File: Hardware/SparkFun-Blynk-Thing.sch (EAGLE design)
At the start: 103 parts, among them IC1 LMV358, Q1 2.5A/30V, Q2 MMBT2222A, Q3 MMBT2222A, U1 MCP73831, U2 ESP8266, U3 AP2112K-3.3V, U4 FT231XS-U, U5 W25Q32FVSS, U6 SI7021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

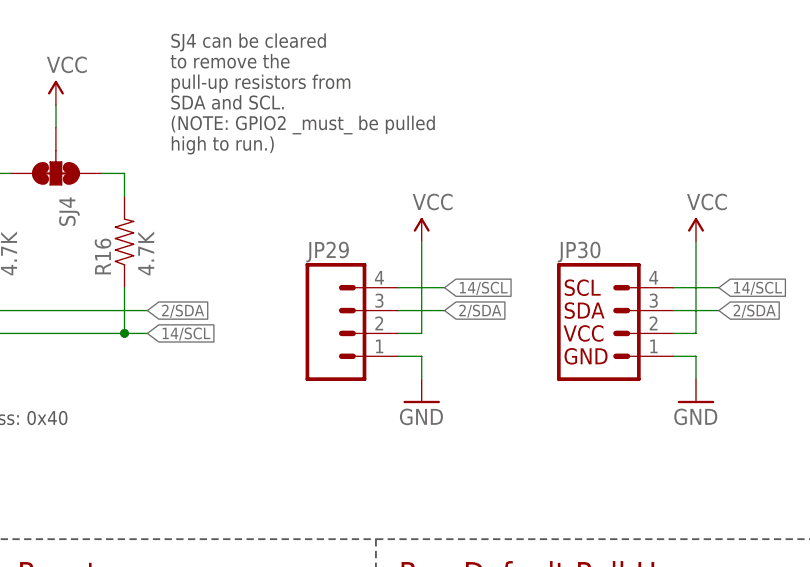
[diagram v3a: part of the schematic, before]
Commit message: Swapping JST connectors on I2C footprint.
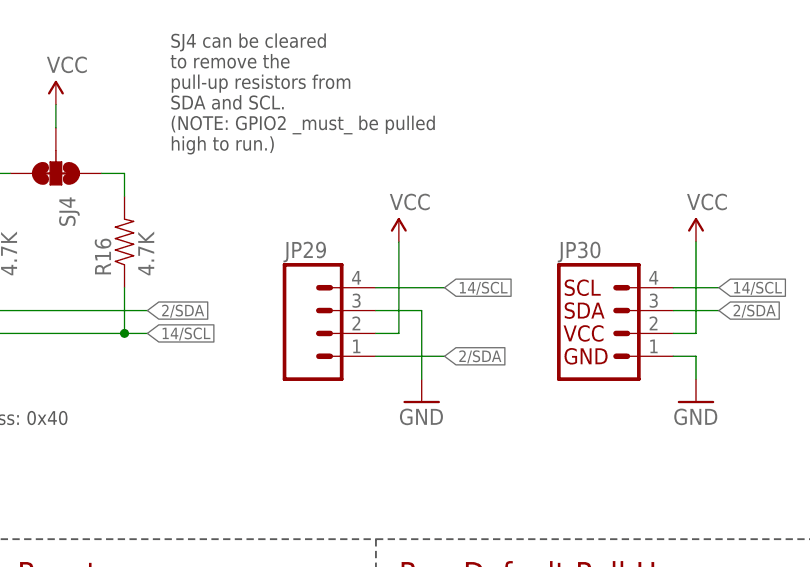
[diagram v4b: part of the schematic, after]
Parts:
- JP29: device SparkFun-Connectors:M04JST -> SparkFun-Connectors:M04JST-PTH-VERT
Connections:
- net 2/SDA: now also JP29.1; no longer JP29.3
- net GND: now also JP29.3; no longer JP29.1
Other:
- moved on the sheet: JP29
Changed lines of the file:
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@@
 <part name="JP4" library="blynk-thing-temp" deviceset="M01" device="ALLIGATOR_HALF" value=""/>
 <part name="JP6" library="blynk-thing-temp" deviceset="M01" device="ALLIGATOR_HALF" value=""/>
-<part name="JP29" library="SparkFun-Connectors" deviceset="M04" device="JST"/>
 <part name="D4" library="SparkFun-LED" deviceset="WS2812B" device="" value="WS2812"/>
 <part name="JP14" library="SparkFun-Connectors" deviceset="M03" device="JST-PTH-VERT">
@@
 <part name="S1" library="SparkFun-Electromechanical" deviceset="SWITCH-MOMENTARY-2" device="SMD-REDUNDANT" value=""/>
 <part name="GND34" library="SparkFun-Aesthetics" deviceset="GND" device=""/>
-<part name="GND38" library="SparkFun-Aesthetics" deviceset="GND" device=""/>
-<part name="SUPPLY19" library="SparkFun-Aesthetics" deviceset="VCC" device=""/>
 <part name="JP13" library="SparkFun-Connectors" deviceset="M01" device="PTH_NO_SILK_YES_STOP"/>
 <part name="JP21" library="SparkFun-Connectors" deviceset="M01" device="PTH_NO_SILK_YES_STOP"/>
@@
 <part name="SUPPLY1" library="SparkFun-Aesthetics" deviceset="VCC" device=""/>
 <part name="GND6" library="SparkFun-Aesthetics" deviceset="GND" device=""/>
+<part name="JP29" library="SparkFun-Connectors" deviceset="M04" device="JST-PTH-VERT"/>
+<part name="SUPPLY3" library="SparkFun-Aesthetics" deviceset="VCC" device=""/>
+<part name="GND42" library="SparkFun-Aesthetics" deviceset="GND" device=""/>
 </parts>
 <sheets>
@@
 <instance part="JP4" gate="G$1" x="165.1" y="101.6"/>
 <instance part="JP6" gate="G$1" x="165.1" y="81.28"/>
-<instance part="JP29" gate="G$1" x="378.46" y="160.02"/>
 <instance part="D4" gate="G$1" x="121.92" y="160.02" rot="MR0"/>
 <instance part="JP14" gate="G$1" x="149.86" y="160.02" smashed="yes" rot="R180">
@@
 <instance part="S1" gate="G$1" x="254" y="175.26"/>
 <instance part="GND34" gate="1" x="261.62" y="170.18"/>
-<instance part="GND38" gate="1" x="386.08" y="152.4"/>
-<instance part="SUPPLY19" gate="G$1" x="386.08" y="170.18"/>
 <instance part="JP13" gate="G$1" x="165.1" y="7.62"/>
 <instance part="JP21" gate="G$1" x="198.12" y="71.12"/>
@@
 <instance part="SUPPLY1" gate="G$1" x="17.78" y="185.42"/>
 <instance part="GND6" gate="1" x="17.78" y="162.56"/>
+<instance part="JP29" gate="G$1" x="375.92" y="160.02"/>
+<instance part="SUPPLY3" gate="G$1" x="383.54" y="170.18"/>
+<instance part="GND42" gate="1" x="386.08" y="152.4"/>
 </instances>
 <busses>
@@
 </segment>
 <segment>
-<pinref part="JP29" gate="G$1" pin="2"/>
-<wire x1="383.54" y1="160.02" x2="386.08" y2="160.02" width="0.1524" layer="91"/>
-<wire x1="386.08" y1="160.02" x2="386.08" y2="170.18" width="0.1524" layer="91"/>
-<pinref part="SUPPLY19" gate="G$1" pin="VCC"/>
-</segment>
-<segment>
 <pinref part="R12" gate="G$1" pin="1"/>
 <pinref part="SUPPLY24" gate="G$1" pin="VCC"/>
@@
 <pinref part="SUPPLY1" gate="G$1" pin="VCC"/>
 <wire x1="17.78" y1="185.42" x2="17.78" y2="182.88" width="0.1524" layer="91"/>
+</segment>
+<segment>
+<pinref part="JP29" gate="G$1" pin="2"/>
+<wire x1="381" y1="160.02" x2="383.54" y2="160.02" width="0.1524" layer="91"/>
+<wire x1="383.54" y1="160.02" x2="383.54" y2="170.18" width="0.1524" layer="91"/>
+<pinref part="SUPPLY3" gate="G$1" pin="VCC"/>
 </segment>
 </net>
@@
 </segment>
 <segment>
-<pinref part="JP29" gate="G$1" pin="1"/>
-<wire x1="383.54" y1="157.48" x2="386.08" y2="157.48" width="0.1524" layer="91"/>
-<wire x1="386.08" y1="157.48" x2="386.08" y2="154.94" width="0.1524" layer="91"/>
-<pinref part="GND38" gate="1" pin="GND"/>
-</segment>
-<segment>
 <pinref part="R11" gate="G$1" pin="2"/>
 <pinref part="GND18" gate="1" pin="GND"/>
@@
 <pinref part="GND6" gate="1" pin="GND"/>
 <wire x1="17.78" y1="165.1" x2="17.78" y2="167.64" width="0.1524" layer="91"/>
+</segment>
+<segment>
+<pinref part="JP29" gate="G$1" pin="3"/>
+<wire x1="381" y1="162.56" x2="386.08" y2="162.56" width="0.1524" layer="91"/>
+<wire x1="386.08" y1="162.56" x2="386.08" y2="154.94" width="0.1524" layer="91"/>
+<pinref part="GND42" gate="1" pin="GND"/>
 </segment>
 </net>
@@
 </segment>
 <segment>
-<pinref part="JP29" gate="G$1" pin="3"/>
-<wire x1="383.54" y1="162.56" x2="388.62" y2="162.56" width="0.1524" layer="91"/>
-<label x="388.62" y="162.56" size="1.27" layer="95" xref="yes"/>
-</segment>
-<segment>
 <pinref part="JP30" gate="G$1" pin="3"/>
 <wire x1="414.02" y1="162.56" x2="419.1" y2="162.56" width="0.1524" layer="91"/>
 <label x="419.1" y="162.56" size="1.27" layer="95" xref="yes"/>
+</segment>
+<segment>
+<pinref part="JP29" gate="G$1" pin="1"/>
+<wire x1="381" y1="157.48" x2="388.62" y2="157.48" width="0.1524" layer="91"/>
+<label x="388.62" y="157.48" size="1.27" layer="95" xref="yes"/>
 </segment>
 </net>
@@
 </segment>
 <segment>
-<pinref part="JP29" gate="G$1" pin="4"/>
-<wire x1="383.54" y1="165.1" x2="388.62" y2="165.1" width="0.1524" layer="91"/>
-<label x="388.62" y="165.1" size="1.27" layer="95" xref="yes"/>
-</segment>
-<segment>
 <pinref part="JP30" gate="G$1" pin="4"/>
 <wire x1="414.02" y1="165.1" x2="419.1" y2="165.1" width="0.1524" layer="91"/>
 <label x="419.1" y="165.1" size="1.27" layer="95" xref="yes"/>
 </segment>
-</net>
+<segment>
+<pinref part="JP29" gate="G$1" pin="4"/>
+<wire x1="381" y1="165.1" x2="388.62" y2="165.1" width="0.1524" layer="91"/>
+<label x="388.62" y="165.1" size="1.27" layer="95" xref="yes"/>
+</segment>
+</net>

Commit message: Updating 4-pin JST PROD_ID
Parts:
- JP29: PROD_ID (none) -> TBD
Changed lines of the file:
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@@
 <part name="SUPPLY1" library="SparkFun-Aesthetics" deviceset="VCC" device=""/>
 <part name="GND6" library="SparkFun-Aesthetics" deviceset="GND" device=""/>
-<part name="JP29" library="SparkFun-Connectors" deviceset="M04" device="JST-PTH-VERT"/>
+<part name="JP29" library="SparkFun-Connectors" deviceset="M04" device="JST-PTH-VERT">
+<attribute name="PROD_ID" value="TBD"/>
+</part>
 <part name="SUPPLY3" library="SparkFun-Aesthetics" deviceset="VCC" device=""/>
 <part name="GND42" library="SparkFun-Aesthetics" deviceset="GND" device=""/>
@@
 <instance part="SUPPLY1" gate="G$1" x="17.78" y="185.42"/>
 <instance part="GND6" gate="1" x="17.78" y="162.56"/>
-<instance part="JP29" gate="G$1" x="375.92" y="160.02"/>
+<instance part="JP29" gate="G$1" x="375.92" y="160.02">
+<attribute name="PROD_ID" x="375.92" y="160.02" size="1.27" layer="96" display="off"/>
+</instance>
 <instance part="SUPPLY3" gate="G$1" x="383.54" y="170.18"/>
 <instance part="GND42" gate="1" x="386.08" y="152.4"/>

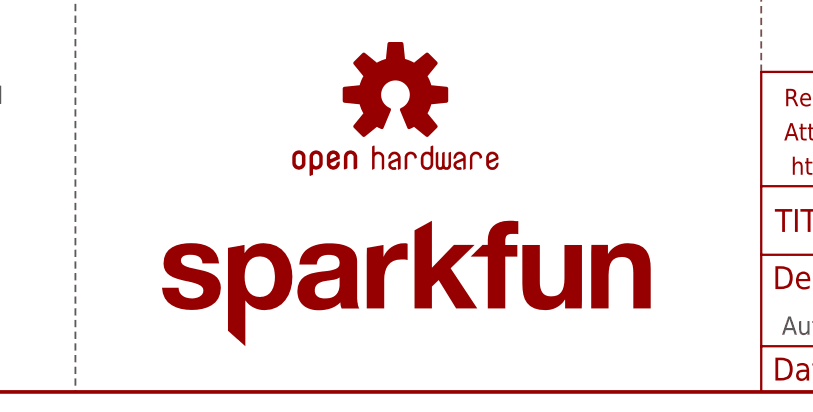
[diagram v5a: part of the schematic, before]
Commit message: Updating board name on silkscreen.
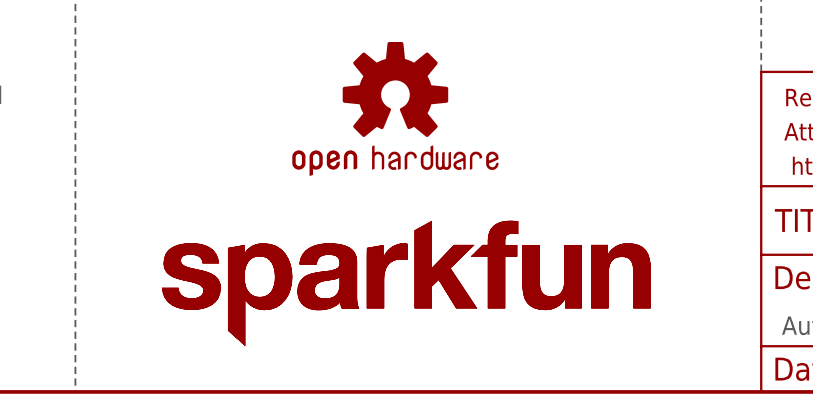
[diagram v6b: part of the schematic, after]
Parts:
- added LOGO3: SFE_LOGO_NAME.3_INCH, SparkFun-Aesthetics:SFE_LOGO_NAME.3_INCH
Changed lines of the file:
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@@
 <grid distance="0.1" unitdist="inch" unit="inch" style="lines" multiple="1" display="no" altdistance="0.01" altunitdist="inch" altunit="inch"/>
 <layers>
-<layer number="1" name="Top" color="4" fill="1" visible="no" active="no"/>
-<layer number="2" name="Route2" color="1" fill="3" visible="no" active="no"/>
-<layer number="3" name="Route3" color="4" fill="3" visible="no" active="no"/>
-<layer number="4" name="Route4" color="1" fill="4" visible="no" active="no"/>
-<layer number="5" name="Route5" color="4" fill="4" visible="no" active="no"/>
-<layer number="6" name="Route6" color="1" fill="8" visible="no" active="no"/>
-<layer number="7" name="Route7" color="4" fill="8" visible="no" active="no"/>
-<layer number="8" name="Route8" color="1" fill="2" visible="no" active="no"/>
-<layer number="9" name="Route9" color="4" fill="2" visible="no" active="no"/>
-<layer number="10" name="Route10" color="1" fill="7" visible="no" active="no"/>
-<layer number="11" name="Route11" color="4" fill="7" visible="no" active="no"/>
-<layer number="12" name="Route12" color="1" fill="5" visible="no" active="no"/>
-<layer number="13" name="Route13" color="4" fill="5" visible="no" active="no"/>
-<layer number="14" name="Route14" color="1" fill="6" visible="no" active="no"/>
-<layer number="15" name="Route15" color="4" fill="6" visible="no" active="no"/>
-<layer number="16" name="Bottom" color="1" fill="1" visible="no" active="no"/>
-<layer number="17" name="Pads" color="2" fill="1" visible="no" active="no"/>
-<layer number="18" name="Vias" color="2" fill="1" visible="no" active="no"/>
-<layer number="19" name="Unrouted" color="6" fill="1" visible="no" active="no"/>
-<layer number="20" name="Dimension" color="15" fill="1" visible="no" active="no"/>
-<layer number="21" name="tPlace" color="16" fill="1" visible="no" active="no"/>
-<layer number="22" name="bPlace" color="14" fill="1" visible="no" active="no"/>
-<layer number="23" name="tOrigins" color="15" fill="1" visible="no" active="no"/>
-<layer number="24" name="bOrigins" color="15" fill="1" visible="no" active="no"/>
-<layer number="25" name="tNames" color="7" fill="1" visible="no" active="no"/>
-<layer number="26" name="bNames" color="7" fill="1" visible="no" active="no"/>
-<layer number="27" name="tValues" color="7" fill="1" visible="no" active="no"/>
-<layer number="28" name="bValues" color="7" fill="1" visible="no" active="no"/>
+<layer number="1" name="Top" color="4" fill="1" visible="yes" active="no"/>
+<layer number="2" name="Route2" color="1" fill="3" visible="yes" active="no"/>
+<layer number="3" name="Route3" color="4" fill="3" visible="yes" active="no"/>
+<layer number="4" name="Route4" color="1" fill="4" visible="yes" active="no"/>
+<layer number="5" name="Route5" color="4" fill="4" visible="yes" active="no"/>
+<layer number="6" name="Route6" color="1" fill="8" visible="yes" active="no"/>
+<layer number="7" name="Route7" color="4" fill="8" visible="yes" active="no"/>
+<layer number="8" name="Route8" color="1" fill="2" visible="yes" active="no"/>
+<layer number="9" name="Route9" color="4" fill="2" visible="yes" active="no"/>
+<layer number="10" name="Route10" color="1" fill="7" visible="yes" active="no"/>
+<layer number="11" name="Route11" color="4" fill="7" visible="yes" active="no"/>
+<layer number="12" name="Route12" color="1" fill="5" visible="yes" active="no"/>
+<layer number="13" name="Route13" color="4" fill="5" visible="yes" active="no"/>
+<layer number="14" name="Route14" color="1" fill="6" visible="yes" active="no"/>
+<layer number="15" name="Route15" color="4" fill="6" visible="yes" active="no"/>
+<layer number="16" name="Bottom" color="1" fill="1" visible="yes" active="no"/>
+<layer number="17" name="Pads" color="2" fill="1" visible="yes" active="no"/>
+<layer number="18" name="Vias" color="2" fill="1" visible="yes" active="no"/>
+<layer number="19" name="Unrouted" color="6" fill="1" visible="yes" active="no"/>
+<layer number="20" name="Dimension" color="15" fill="1" visible="yes" active="no"/>
+<layer number="21" name="tPlace" color="16" fill="1" visible="yes" active="no"/>
+<layer number="22" name="bPlace" color="14" fill="1" visible="yes" active="no"/>
+<layer number="23" name="tOrigins" color="15" fill="1" visible="yes" active="no"/>
+<layer number="24" name="bOrigins" color="15" fill="1" visible="yes" active="no"/>
+<layer number="25" name="tNames" color="7" fill="1" visible="yes" active="no"/>
+<layer number="26" name="bNames" color="7" fill="1" visible="yes" active="no"/>
+<layer number="27" name="tValues" color="7" fill="1" visible="yes" active="no"/>
+<layer number="28" name="bValues" color="7" fill="1" visible="yes" active="no"/>
 <layer number="29" name="tStop" color="7" fill="3" visible="no" active="no"/>
 <layer number="30" name="bStop" color="7" fill="6" visible="no" active="no"/>
@@
 <layer number="35" name="tGlue" color="7" fill="4" visible="no" active="no"/>
 <layer number="36" name="bGlue" color="7" fill="5" visible="no" active="no"/>
-<layer number="37" name="tTest" color="7" fill="1" visible="no" active="no"/>
-<layer number="38" name="bTest" color="7" fill="1" visible="no" active="no"/>
+<layer number="37" name="tTest" color="7" fill="1" visible="yes" active="no"/>
+<layer number="38" name="bTest" color="7" fill="1" visible="yes" active="no"/>
 <layer number="39" name="tKeepout" color="4" fill="11" visible="no" active="no"/>
 <layer number="40" name="bKeepout" color="1" fill="11" visible="no" active="no"/>
@@
 <layer number="44" name="Drills" color="7" fill="1" visible="no" active="no"/>
 <layer number="45" name="Holes" color="7" fill="1" visible="no" active="no"/>
-<layer number="46" name="Milling" color="3" fill="1" visible="no" active="no"/>
-<layer number="47" name="Measures" color="7" fill="1" visible="no" active="no"/>
-<layer number="48" name="Document" color="7" fill="1" visible="no" active="no"/>
-<layer number="49" name="Reference" color="7" fill="1" visible="no" active="no"/>
-<layer number="50" name="dxf" color="7" fill="1" visible="no" active="no"/>
-<layer number="51" name="tDocu" color="6" fill="1" visible="no" active="no"/>
-<layer number="52" name="bDocu" color="7" fill="1" visible="no" active="no"/>
-<layer number="53" name="tGND_GNDA" color="7" fill="9" visible="no" active="no"/>
-<layer number="54" name="bGND_GNDA" color="1" fill="9" visible="no" active="no"/>
-<layer number="56" name="wert" color="7" fill="1" visible="no" active="no"/>
-<layer number="57" name="tCAD" color="7" fill="1" visible="no" active="no"/>
-<layer number="59" name="tCarbon" color="7" fill="1" visible="no" active="no"/>
-<layer number="60" name="bCarbon" color="7" fill="1" visible="no" active="no"/>
+<layer number="46" name="Milling" color="3" fill="1" visible="yes" active="no"/>
+<layer number="47" name="Measures" color="7" fill="1" visible="yes" active="no"/>
+<layer number="48" name="Document" color="7" fill="1" visible="yes" active="no"/>
+<layer number="49" name="Reference" color="7" fill="1" visible="yes" active="no"/>
+<layer number="50" name="dxf" color="7" fill="1" visible="yes" active="no"/>
+<layer number="51" name="tDocu" color="6" fill="1" visible="yes" active="no"/>
+<layer number="52" name="bDocu" color="7" fill="1" visible="yes" active="no"/>
+<layer number="53" name="tGND_GNDA" color="7" fill="9" visible="yes" active="no"/>
+<layer number="54" name="bGND_GNDA" color="1" fill="9" visible="yes" active="no"/>
+<layer number="56" name="wert" color="7" fill="1" visible="yes" active="no"/>
+<layer number="57" name="tCAD" color="7" fill="1" visible="yes" active="no"/>
+<layer number="59" name="tCarbon" color="7" fill="1" visible="yes" active="no"/>
+<layer number="60" name="bCarbon" color="7" fill="1" visible="yes" active="no"/>
 <layer number="90" name="Modules" color="5" fill="1" visible="yes" active="yes"/>
 <layer number="91" name="Nets" color="2" fill="1" visible="yes" active="yes"/>
@@
 <part name="SUPPLY3" library="SparkFun-Aesthetics" deviceset="VCC" device=""/>
 <part name="GND42" library="SparkFun-Aesthetics" deviceset="GND" device=""/>
+<part name="LOGO3" library="SparkFun-Aesthetics" deviceset="SFE_LOGO_NAME" device=".3_INCH" value="SFE_LOGO_NAME.3_INCH"/>
 </parts>
 <sheets>
@@
 <instance part="SUPPLY3" gate="G$1" x="383.54" y="170.18"/>
 <instance part="GND42" gate="1" x="386.08" y="152.4"/>
+<instance part="LOGO3" gate="G$1" x="261.62" y="5.08"/>
 </instances>
 <busses>
